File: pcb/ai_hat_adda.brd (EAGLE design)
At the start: 65.1 x 56 mm, 48 parts, among them J1 1X03ST, J2 1X03ST, J3 1X02ST, J4 1X02ST, K1 2X20-RPI, U1 24LC32A, U2 ADS1115, U3 MCP4725, U4 MCP4725

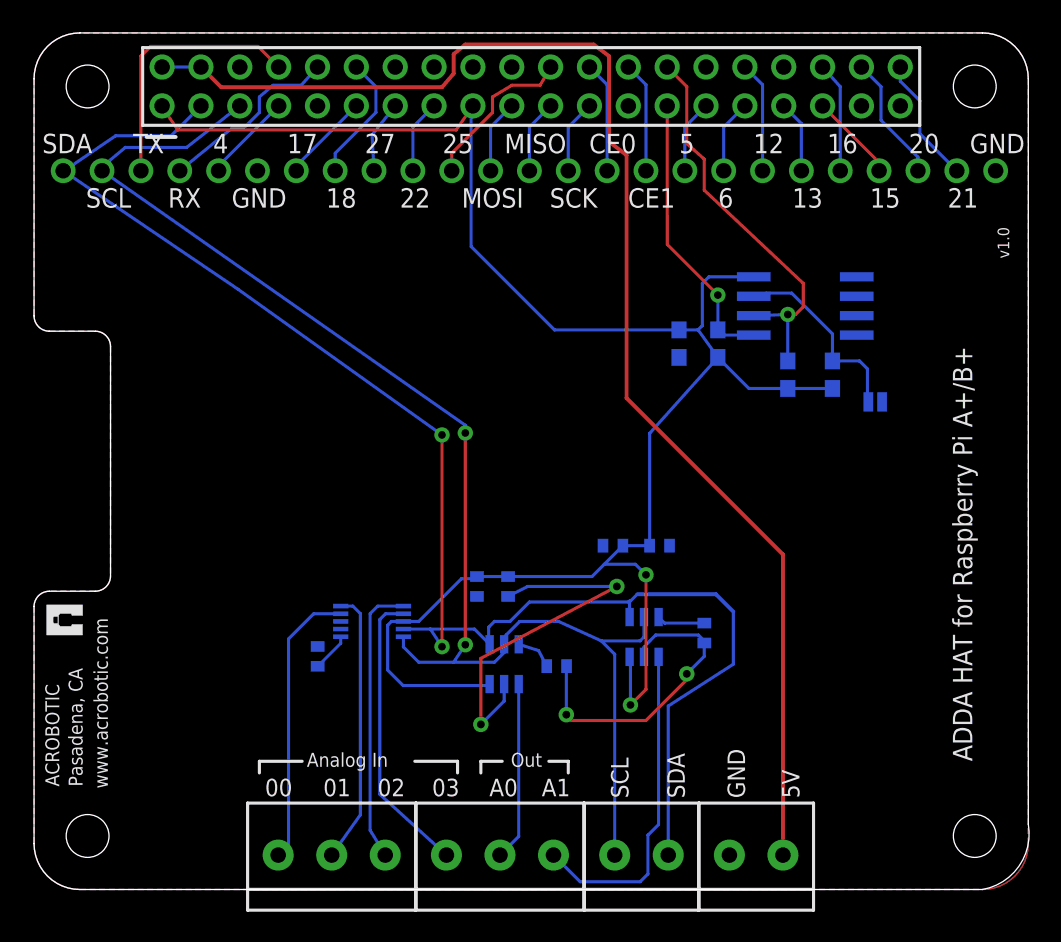
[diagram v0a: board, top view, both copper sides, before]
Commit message: minor silkscreen updates. added 3V3 output.
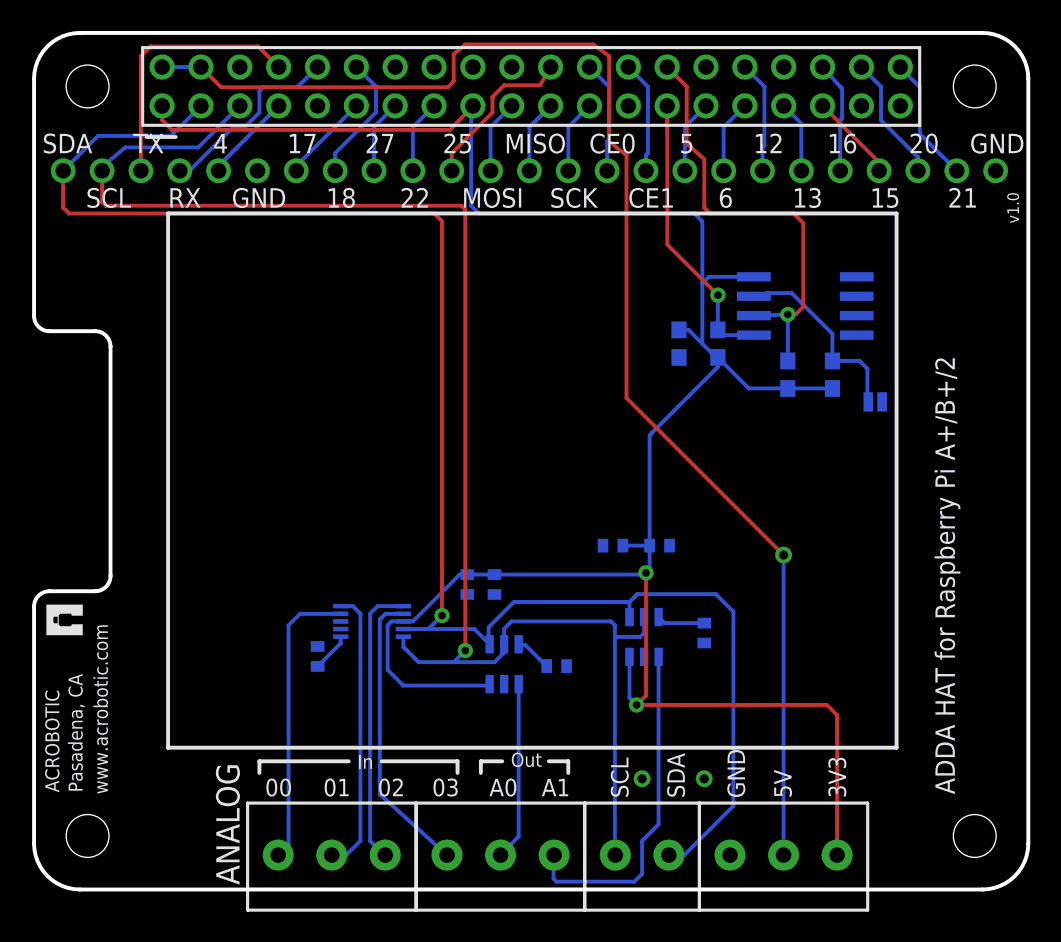
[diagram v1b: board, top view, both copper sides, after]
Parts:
- J3: value 1X02ST -> 1X03ST; device Ai_Connectors:1X02-ST -> Ai_Connectors:1X03-ST
- moved J3 1.79 mm to (49.0, 2.25)
- moved C3 0.90 mm to (30.1, 19.9)
- moved C2 0.65 mm to (28.3, 19.9)
- moved U$10 0.63 mm to (3.17, 18.5)
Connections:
- net 3V3: now also J3.3
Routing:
- net GND: track 45.6 -> 0.15 mm, vias 4 -> 2
- net 3V3: track 124.0 -> 148.5 mm
- net SCL: track 89.9 -> 101.9 mm, vias 2 -> 1
- net SDA: track 99.8 -> 109.1 mm, vias 2 -> 1
- net ID_SC: track 26.0 -> 29.1 mm
- net AIN1: track 17.9 -> 18.6 mm
- net AOUT1: track 21.6 -> 22.3 mm
- net AIN0: track 18.5 -> 19.0 mm
- net 5V: track 89.0 -> 89.2 mm, vias 0 -> 1
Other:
- board size 65.1 x 56 mm -> 65 x 56 mm
- board text added: "3V3"
- board text added: "ADDA HAT for Raspberry Pi A+/B+/2"
- board text added: "ANALOG"
- board text added: "In"
- board text removed: "ADDA HAT for Raspberry Pi A+/B+"
- board text removed: "Analog In"

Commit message: updating
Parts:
- K1: value 2X20-RPI -> 2X20-RPI-ALT; device Ai_Connectors:2X20-RPI -> Ai_Connectors:2X20-RPI-ALT
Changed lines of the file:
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@@
 <setting verticaltext="up"/>
 </settings>
-<grid distance="10" unitdist="mil" unit="mil" style="lines" multiple="1" display="yes" altdistance="0.025" altunitdist="inch" altunit="inch"/>
+<grid distance="50" unitdist="mil" unit="mil" style="lines" multiple="1" display="yes" altdistance="0.025" altunitdist="inch" altunit="inch"/>
 <layers>
 <layer number="1" name="Top" color="4" fill="1" visible="yes" active="yes"/>
@@
 <text x="16.51" y="45.847" size="1.27" layer="21" font="vector" ratio="10" rot="R180">GND</text>
 <text x="64.77" y="49.403" size="1.27" layer="21" font="vector" ratio="10" rot="R180">GND</text>
-<wire x1="12.065" y1="2.54" x2="40.005" y2="2.54" width="0.254" layer="30"/>
-<wire x1="47.625" y1="2.54" x2="52.705" y2="2.54" width="0.254" layer="30"/>
-<wire x1="47.625" y1="5.08" x2="52.705" y2="5.08" width="0.254" layer="30"/>
 <text x="60.198" y="6.223" size="1.27" layer="21" font="vector" ratio="10" rot="R90">ADDA HAT for Raspberry Pi A+/B+/2</text>
 <text x="63.627" y="45.593" size="0.762" layer="21" font="vector" ratio="10" rot="R270">v1.0</text>
@@
 </autorouter>
 <elements>
-<element name="K1" library="Ai_Connectors" package="2X20-RPI" value="2X20-RPI" x="32.5" y="52.5" smashed="yes"/>
+<element name="K1" library="Ai_Connectors" package="2X20-RPI-ALT" value="2X20-RPI-ALT" x="32.5" y="52.5" smashed="yes"/>
 <element name="U1" library="Ai_IC" package="SO08-EIAJ" value="24LC32A" x="50.407" y="38.149" smashed="yes" rot="MR270"/>
 <element name="R1" library="Ai_Passives" package="RES-0603" value="3k9" x="49.276" y="33.655" smashed="yes" rot="MR270">

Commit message: updating
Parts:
- moved C5 13.7 mm to (27.3, 20.7), turned to 270 degrees
- moved C4 12.2 mm to (25.8, 20.7), turned to 90 degrees
- moved U4 9.32 mm to (30.7, 14.7), turned to 0 degrees
- moved C3 8.54 mm to (36.4, 14.2)
- moved U3 8.00 mm to (38.7, 14.9), turned to 0 degrees
- moved C1 6.87 mm to (45.7, 41.6), turned to 0 degrees
- moved C2 5.72 mm to (28.4, 14.2)
- moved U$10 2.05 mm to (2.41, 16.6), turned to 90 degrees
- moved R6 2.01 mm to (42.7, 15.1)
- moved J1 1.29 mm to (20.8, 2.30)
- moved U2 1.02 mm to (23.1, 17.5)
- moved R4 1.02 mm to (19.6, 15.2)
- moved J2 0.75 mm to (31.2, 2.30)
- moved R5 0.63 mm to (34.5, 15.1), turned to 90 degrees
- moved J3 0.25 mm to (48.8, 2.30)
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- renumbered U1 to EEPROM
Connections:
- net 3V3: now also R5.1
- net GND: no longer R5.1
- net N$2: now also U3.6; no longer U4.6
- net N$4: now also U4.6; no longer U3.6
- net SCL: now also J4.2; no longer J4.1
- net SDA: now also J4.1; no longer J4.2
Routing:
- net SDA: track 109.1 -> 119.2 mm
- net AOUT0: track 11.7 -> 18.9 mm
- net 3V3: track 148.5 -> 154.4 mm, vias 2 -> 0
- net SCL: track 101.9 -> 97.2 mm
- net GND: track 0.15 -> 2.99 mm, vias 2 -> 0
- net AOUT1: track 22.3 -> 20.5 mm
- net AIN1: track 18.6 -> 17.7 mm
- net AIN2: track 18.6 -> 19.3 mm
- net AIN0: track 19.0 -> 19.7 mm
- net N$4: track 2.40 -> 2.97 mm
- net AIN3: track 19.1 -> 19.6 mm
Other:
- board text added: "ADC: 4-Channel (I2C: 0x48) DAC: 2-Channel (I2C: 0x60 (A0) 0x61 (A1))"
- board text added: "EEPROM CFG"
- board text added: "S.P.-v1.2"
- board text removed: "EEPROM"
- board text removed: "v1.0"

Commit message: fixed tracing problem.
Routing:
- net AOUT1: track 20.5 -> 19.7 mm
- net AOUT0: track 18.9 -> 18.3 mm
- net GND: vias 0 -> 2
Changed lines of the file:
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@@
 <setting verticaltext="up"/>
 </settings>
-<grid distance="2.5" unitdist="mil" unit="mil" style="lines" multiple="1" display="yes" altdistance="0.025" altunitdist="inch" altunit="inch"/>
+<grid distance="5" unitdist="mil" unit="mil" style="lines" multiple="1" display="yes" altdistance="0.025" altunitdist="inch" altunit="inch"/>
 <layers>
 <layer number="1" name="Top" color="4" fill="1" visible="yes" active="yes"/>
@@
 <wire x1="19.558" y1="17.272" x2="19.812" y2="17.526" width="0.254" layer="16"/>
 <wire x1="19.812" y1="17.526" x2="21.064" y2="17.526" width="0.254" layer="16"/>
+<via x="31.242" y="10.16" extent="1-16" drill="0.508"/>
+<via x="25.527" y="12.319" extent="1-16" drill="0.508"/>
 </signal>
 <signal name="N$3">
@@
 <wire x1="27.559" y1="17.907" x2="26.678" y2="17.026" width="0.3048" layer="16"/>
 <wire x1="26.678" y1="17.026" x2="25.164" y2="17.026" width="0.254" layer="16"/>
-<wire x1="27.559" y1="17.907" x2="27.559" y2="4.953" width="0.3048" layer="1"/>
-<wire x1="27.559" y1="4.953" x2="28.448" y2="4.064" width="0.3048" layer="1"/>
-<wire x1="28.448" y1="4.064" x2="37.465" y2="4.064" width="0.3048" layer="1"/>
-<wire x1="37.465" y1="4.064" x2="38.25" y2="3.279" width="0.3048" layer="1"/>
+<wire x1="27.559" y1="17.907" x2="27.559" y2="6.223" width="0.3048" layer="1"/>
+<wire x1="27.559" y1="6.223" x2="28.448" y2="5.334" width="0.3048" layer="1"/>
+<wire x1="28.448" y1="5.334" x2="37.465" y2="5.334" width="0.3048" layer="1"/>
+<wire x1="37.465" y1="5.334" x2="38.25" y2="4.549" width="0.3048" layer="1"/>
 <wire x1="37.785" y1="16.1591" x2="37.785" y2="14.92" width="0.3048" layer="16"/>
 <wire x1="37.785" y1="14.92" x2="38.1" y2="14.605" width="0.3048" layer="16"/>
@@
 <wire x1="38.481" y1="4.064" x2="38.25" y2="3.833" width="0.3048" layer="16"/>
 <wire x1="38.25" y1="2.3" x2="38.25" y2="3.833" width="0.3048" layer="16"/>
-<wire x1="38.25" y1="3.279" x2="38.25" y2="2.3" width="0.3048" layer="1"/>
+<wire x1="38.25" y1="4.549" x2="38.25" y2="2.3" width="0.3048" layer="1"/>
 <wire x1="29.784" y1="16.0321" x2="28.8591" y2="16.0321" width="0.3048" layer="16"/>
 <wire x1="28.8591" y1="16.0321" x2="28.829" y2="16.002" width="0.3048" layer="16"/>
@@
 <contactref element="J2" pad="2"/>
 <wire x1="31.25" y1="2.3" x2="31.283" y2="2.3" width="0.3048" layer="16"/>
-<wire x1="31.283" y1="2.3" x2="31.684" y2="2.701" width="0.3048" layer="16"/>
+<wire x1="31.283" y1="2.3" x2="32.7" y2="3.59" width="0.3048" layer="16"/>
 <contactref element="U3" pad="1"/>
-<wire x1="31.684" y1="2.701" x2="31.684" y2="11.491" width="0.3048" layer="16"/>
-<wire x1="31.684" y1="11.491" x2="32.131" y2="11.938" width="0.3048" layer="16"/>
-<wire x1="32.131" y1="11.938" x2="39.116" y2="11.938" width="0.3048" layer="16"/>
+<wire x1="32.7" y1="3.59" x2="32.7" y2="11.491" width="0.3048" layer="16"/>
+<wire x1="32.7" y1="11.491" x2="33.147" y2="11.938" width="0.3048" layer="16"/>
+<wire x1="33.147" y1="11.938" x2="39.116" y2="11.938" width="0.3048" layer="16"/>
 <wire x1="39.116" y1="11.938" x2="39.685" y2="12.507" width="0.3048" layer="16"/>
 <wire x1="39.685" y1="13.5589" x2="39.685" y2="12.507" width="0.3048" layer="16"/>
@@
 <wire x1="34.163" y1="0.762" x2="29.845" y2="0.762" width="0.3048" layer="16"/>
 <wire x1="29.845" y1="0.762" x2="29.591" y2="1.016" width="0.3048" layer="16"/>
-<wire x1="29.591" y1="1.016" x2="29.591" y2="11.557" width="0.3048" layer="16"/>
-<wire x1="29.591" y1="11.557" x2="30.099" y2="12.065" width="0.3048" layer="16"/>
-<wire x1="31.684" y1="13.4319" x2="31.684" y2="12.38" width="0.3048" layer="16"/>
-<wire x1="31.684" y1="12.38" x2="31.369" y2="12.065" width="0.3048" layer="16"/>
-<wire x1="31.369" y1="12.065" x2="30.099" y2="12.065" width="0.3048" layer="16"/>
+<wire x1="29.591" y1="1.016" x2="29.591" y2="10.16" width="0.3048" layer="16"/>
+<wire x1="31.684" y1="13.4319" x2="31.684" y2="12.253" width="0.3048" layer="16"/>
+<wire x1="31.684" y1="12.253" x2="29.591" y2="10.16" width="0.3048" layer="16"/>
 <wire x1="34.75" y1="2.3" x2="34.417" y2="1.967" width="0.3048" layer="16"/>
 <wire x1="34.417" y1="1.967" x2="34.417" y2="1.016" width="0.3048" layer="16"/>

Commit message: updating
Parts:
- added FRAME1: FRAME-LETTER, Ai_Miscellany:CREATIVE-COMMONS
- C1: value 100nF -> 0.1uF
- R1, R2: value 3k9 -> 3K9
- R3: value 1k -> 1K
- moved U$9 4.50 mm to (1.91, 12.3)
- moved U$10 4.46 mm to (2.03, 12.2)
- moved J3 3.10 mm to (51.9, 2.30)
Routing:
- net 5V: track 89.0 -> 90.3 mm
- net 3V3: track 154.4 -> 155.6 mm
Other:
- outline, holes or cut-outs redrawn
- board text added: "19"
- board text added: "@AcrobotSP"
- board text removed: "15"
